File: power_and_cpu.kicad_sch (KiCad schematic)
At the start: 256 parts, among them J1 CPU1 USB, J10 AUX GPIO 1, J11 CAN2 PLUG, J12 Conn_01x06, J13 ADC AUX 2, J14 AUX GPIO 2, J15 AUX Encoder, J16 Conn_01x07, J17 CAN Output, J2 CAN Input, J21 Power Input, J3 Encoder 1, J4 Encoder 2, J5 Conn_01x06, J6 CPU2 USB, J7 Conn_01x02, J9 ADC AUX 1, Q7 Q_NMOS_GSD, SW1 SW_MEC_5G, SW2 SW_MEC_5G, SW3 CONFIG SWITCH, U10 TXS0101DCKR, U11 TLV1117LV33DCYR, U12 W25Q128JVSIQ, U13 W25Q128JVSIQ, U15 RP2040, U17 isolator, U18 MCP2515-xSO, U19 RP2040, U22 ADS7822U, U23 SN74LVC1G07QDCKTQ1, U24 MT2492, U25 NCP1117-5_SOT223, U26 ADC081S021CISD/NOPB, U27 USBLC6-2P6, U28 USBLC6-2P6, U29 USBLC6-4SC6, U3 USBLC6-4SC6, U30 USBLC6-4SC6, U31 USBLC6-4SC6, U32 TLV1117LV33DCYR, U33 TX4139, U34 LTV-208, U43 USBLC6-4SC6, U6 SN74LVC1G07QDCKTQ1, U9 ADC081S021CISD/NOPB, Y1 12MHz, Y2 12MHz, Y3 16MHz

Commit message: Rev 3.1 updated files. ordered Nov 2 2023
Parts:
- removed J7: Conn_01x02, parts:BOOMELE-2510-2A _1x02_P2.54mm_Vertical, symbol Connector_Generic:Conn_01x02
- removed U25: NCP1117-5_SOT223, Package_TO_SOT_SMD:SOT-223-3_TabPin2, symbol Regulator_Linear:NCP1117-3.3_SOT223
- added J8: Estop Conn, parts:BOOMELE-2510-3A_1x03_P2.54mm_Vertical, symbol Connector_Generic:Conn_01x03
- added JP1: SolderJumper_2_Open, Jumper:SolderJumper-2_P1.3mm_Open_RoundedPad1.0x1.5mm, symbol Jumper:SolderJumper_2_Open
- C87, C88, C89, C90, C91, C92: value C -> 22nF; LCSC (none) -> C77069; now fitted; now in the parts list
- C98: LCSC C106217 -> C779971
- D28, D29, D30, D32: LCSC C129213 -> C2841409
- D39: Digikey 67-1696-1-ND -> (none); LCSC C5137318 -> C84261; MPN SML-LX1206SOC-TR -> (none)
- J12, J3, J4, J5: LCSC C140771 -> C2982035
- J17, J2: now left out of the parts list
- J21: LCSC (none) -> C98733; now in the parts list
- R99: LCSC C22773 -> C2933129
- TP22: LCSC C238130 -> C5199800
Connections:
- net ADC_CS3 is gone; now on net ADC_CS2: U19.5 (GPIO3), U26.6 (~{CS})
- net ADC_CS2: no longer U19.3 (GPIO1), U9.6 (~{CS})
- net CAN0_N: no longer JP2.1 (A)
- net CANH0_P_JP: no longer JP2.2 (B)
- net ESTOP_SWITCH_IN: now also J8.3 (Pin_3)
- net ESTOP_SWITCH_OUT: now also J8.1 (Pin_1)
- net GND: now also J21.1 (Pin_1), JP2.1 (A), JP1.1 (A); no longer C87.1, C88.2, C89.2, C90.1, C91.1, C92.1, J21.2 (Pin_2)
- net VMOT: now also J21.2 (Pin_2); no longer J21.1 (Pin_1)
- net GPIO28_ADC2_2 renamed TH_MOTOR1
- net GPIO29_ADC3_2 renamed TH_MOTOR2
- net VDC_DATA renamed GPIO23
- new net ADC_CS1: U19.3 (GPIO1), U9.6 (~{CS})
- new net ENC1_JP: C87.1, C88.2, C89.2, JP1.2 (B)
- new net ENC2_JP: C90.1, C91.1, C92.1, JP2.2 (B)
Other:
- note added: "Jumpers enable additional filtering for hall sensors."
- note removed: "Backup footprint if new 5v switcher does not work properly."
- note removed: "These DNP caps are optional filter caps for hall sensors."
- moved on the sheet: R74

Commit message: Update to Rev 3.2. Probably okay to order this rev.
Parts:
- removed TP1, TP3: TestPoint, TestPoint:TestPoint_Pad_1.0x1.0mm, symbol Connector:TestPoint
- added C67: 100n, Capacitor_SMD:C_0603_1608Metric, symbol Device:C
- added D45: 10V Zener, Diode_SMD:D_SOD-123, symbol Device:D_Zener
- added D46: 7.5V Zener, Diode_SMD:D_SOD-123, symbol Device:D_Zener
- added Q10: AO3401A, Package_TO_SOT_SMD:SOT-23, symbol Transistor_FET:AO3401A
- added Q11: L2N7002SWT1G, Package_TO_SOT_SMD:SOT-323_SC-70, symbol Transistor_FET:AO3400A
- added Q8: Q_NMOS_GSD, Package_TO_SOT_SMD:SOT-23, symbol Device:Q_NMOS_GSD
- added Q9: AO3400A, Package_TO_SOT_SMD:SOT-23, symbol Transistor_FET:AO3400A
- added R100: 120R, Resistor_SMD:R_0603_1608Metric, symbol MotorController:TAYLOR_RESISTOR
- added R102: 20k, Resistor_SMD:R_0603_1608Metric, symbol MotorController:TAYLOR_RESISTOR
- added R103, R106: 100k, Resistor_SMD:R_0603_1608Metric, symbol MotorController:TAYLOR_RESISTOR
- added R104, R107, R137, R138: 10k, Resistor_SMD:R_0603_1608Metric, symbol MotorController:TAYLOR_RESISTOR
- added SW4: SW_DIP_x01, parts:SW-SMD_DSHP01TSGER, symbol Switch:SW_DIP_x01
- added U16: ~, Package_SO:SOP-4_4.4x2.6mm_P1.27mm, symbol Isolator:SFH617A-1X007T
- added U25: SN74LVC1G07QDCKTQ1, Package_TO_SOT_SMD:SOT-353_SC-70-5, symbol acorn-motherboard:SN74LVC1G07QDCKTQ1
- added U35: PCA9557PW, Package_SO:TSSOP-16_4.4x5mm_P0.65mm, symbol Interface_Expansion:PCA9557PW
- U26, U9: symbol 2022-06-16_01-48-54:ADC081S021CISD/NOPB -> 2022-06-16_01-48-54:ADC081S021CISD/NOPB
- renumbered C26 to C120
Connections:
- net +12V: now also D46.1 (K), Q10.2 (S), R106.1; no longer U24.4 (EN)
- net +3V3: now also C67.1, R137.2, U25.2 (A), U25.5 (VCC), U35.16 (VDD)
- net +5V_ISO: now also R100.1
- net GND: now also C67.2, D45.2 (A), Q11.2 (S), Q8.2 (S), Q9.2 (S), R103.2, R107.2, R138.2, U16.3, U25.3 (GND), U35.3 (A0), U35.4 (A1), U35.5 (A2), U35.8 (VSS); no longer D33.1 (GND), D34.1 (GND), D35.1 (GND)
- net GND_ISO: now also U16.2
- net ID1: now also U35.6 (IO0); no longer U19.29 (GPIO18)
- net ID2: now also U35.7 (IO1); no longer U19.30 (GPIO19)
- net ID3: now also U35.9 (IO2); no longer U19.35 (GPIO23)
- net VMOT: now also R102.1
- net /LED_EN: now also U25.1 (/OE)
- net ~{EN}: now reaches U33.6 (EN)
- net ~{EN}: now also SW4.2
- net 12V_POK: now reaches U33.7 (POK)
- net 12V_POK: now also U24.4 (EN), R106.2
- net DRIVER_ENABLE: now reaches U19.7 (GPIO5)
- net DRIVER_ENABLE: now also Q9.1 (G), R107.1
- new net: D45.1 (K), Q8.1 (G), R102.2, R103.1, U16.4
- new net: Q9.3 (D), R104.2
- new net: R100.2, U16.1
- new net: Q11.1 (G), R138.1, U25.4 (Y)
- new net: R137.1, U35.15 (~{RESET})
- new net: D46.2 (A), Q10.1 (G), R104.1
- new net: Q8.3 (D), SW4.1
- new net 12V_SWITCHED: Q10.3 (D)
- new net SCL1: U19.30 (GPIO19), U35.1 (SCL)
- new net SDA1: U19.29 (GPIO18), U35.2 (SDA)
- new net WS2812_SINK: D33.1 (GND), D34.1 (GND), D35.1 (GND), Q11.3 (D)
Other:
- moved on the sheet: C19, C42, C43, C44, C45, C46, C47, C48, C49, C50, C51, C52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

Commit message: Latest updates to module based design.
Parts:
- removed D46: 7.5V Zener, Diode_SMD:D_SOD-123, symbol Device:D_Zener
- removed H1, H2, H6, H7, H8: MountingHole, RP2040_minimal:MountingHole_3.9mm_Plastite_#6, symbol Mechanical:MountingHole
- removed J16: Conn_01x07, Connector_PinHeader_2.54mm:PinHeader_2x04_P2.54mm_Vertical, symbol Connector_Generic:Conn_01x07
- removed J21: Power Input, Connector_AMASS:AMASS_XT60-F_1x02_P7.20mm_Vertical, symbol Connector_Generic:Conn_01x02
- removed Q10: AO3401A, Package_TO_SOT_SMD:SOT-23, symbol Transistor_FET:AO3401A
- removed Q9: AO3400A, Package_TO_SOT_SMD:SOT-23, symbol Transistor_FET:AO3400A
- removed R104, R107: 10k, Resistor_SMD:R_0603_1608Metric, symbol MotorController:TAYLOR_RESISTOR
- removed TH1, TH2: Thermistor 10k, Resistor_SMD:R_0603_1608Metric, symbol Device:Thermistor_NTC
- removed TP49, TP51: TestPoint, TestPoint:TestPoint_Pad_D2.0mm, symbol Connector:TestPoint
- added JP10: SolderJumper_3_Open, Jumper:SolderJumper-3_P1.3mm_Open_RoundedPad1.0x1.5mm, symbol Jumper:SolderJumper_3_Open
- added JP4, JP5, JP8, JP9: SolderJumper_2_Open, Jumper:SolderJumper-2_P1.3mm_Open_RoundedPad1.0x1.5mm, symbol Jumper:SolderJumper_2_Open
- added U1, U2: ~, driver_module:driver_module, symbol driver_module:Driver
- added U4: TXS0101DCKR, Package_TO_SOT_SMD:SOT-363_SC-70-6, symbol MotorBuck:level_shifter
- C120: footprint Capacitor_THT:CP_Radial_D8.0mm_P3.50mm -> Capacitor_SMD:CP_Elec_8x10.5; LCSC C2887234 -> C5246568
- J10, J13, J14, J9: footprint parts:BOOMELE-2510-3A_1x03_P2.54mm_Vertical -> parts:CONN-TH_3P-P2.54_HCTL_HC-2510-3AW; LCSC C509148 -> C2982042
- J15: footprint parts:BOOMELE-2510-5A _1x05_P2.54mm_Vertical -> parts:CONN-TH_5P-P2.54_HCTL_HC-2510-5AW; LCSC C27544 -> C2982044
- SW1, SW2: footprint parts:SW_TS_1101_C_W -> parts:KEY-SMD_1TS002G; LCSC C318938 -> C319375
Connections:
- net +12V: now also U1.5 (+12V), U2.5 (+12V)
- net +3.3VA: now also U1.7 (+3V3), U2.7 (+3V3)
- net +3V3: now also JP10.1 (A), U4.1 (VCCA), U4.5 (OE); no longer J15.1 (Pin_1), TP34.1
- net +5V: now also JP10.3 (B)
- net AUX3_SCK: now also U4.3 (A); no longer J15.4 (Pin_4), TP37.1
- net GND: now also JP4.1 (A), JP5.1 (A), JP8.1 (A), JP9.1 (A), U1.1 (GND), U1.12 (GND), U1.2 (Thermistor), U1.21 (GND), U1.22 (GND), U1.25 (GND), U1.26 (GND), U2.1 (GND), U2.12 (GND), U2.2 (Thermistor), U2.21 (GND), U2.22 (GND), U2.25 (GND), U2.26 (GND), U4.2 (GND)
- net M1A_PWM_H: now also U1.16 (PWM_A_H)
- net M1A_PWM_L\: now also U1.18 (PWM_A_L\)
- net M1A_SENSE: now also U1.19 (SENSE_A)
- net M1B_PWM_H: now also U1.20 (PWM_B_H)
- net M1B_PWM_L\: now also U1.17 (PWM_B_L\)
- net M1C_PWM_H: now also U1.8 (PWM_C_H)
- net M1C_PWM_L\: now also U1.6 (PWM_C_L\)
- net M1C_SENSE: now also U1.9 (SENSE_C)
- net M2A_PWM_H: now also U2.16 (PWM_A_H)
- net M2A_PWM_L\: now also U2.18 (PWM_A_L\)
- net M2A_SENSE: now also U2.19 (SENSE_A)
- net M2B_PWM_H: now also U2.20 (PWM_B_H)
- net M2B_PWM_L\: now also U2.17 (PWM_B_L\)
- net M2C_PWM_H: now also U2.8 (PWM_C_H)
- net M2C_PWM_L\: now also U2.6 (PWM_C_L\)
- net M2C_SENSE: now also U2.9 (SENSE_C)
- net VMOT: now also U1.11 (VMOT), U1.13 (VMOT), U1.23 (VMOT), U1.24 (VMOT), U2.11 (VMOT), U2.13 (VMOT), U2.23 (VMOT), U2.24 (VMOT)
- net Bridge_TH_1: now reaches R45.1, U9.3 (VIN)
- net Bridge_TH_1: now also U1.2 (Thermistor)
- net Bridge_TH_2: now reaches R21.1, U26.3 (VIN)
- net Bridge_TH_2: now also U2.2 (Thermistor)
- net DRIVER_ENABLE: no longer names the net of U19.7 (GPIO5)
- removed net ENC1_JP: C87.1, C88.2, C89.2, JP1.2 (B)
- removed net ENC2_JP: C90.1, C91.1, C92.1, JP2.2 (B)
- new net: C90.1, JP4.2 (B)
- new net: C89.2, JP2.2 (B)
- new net: C91.1, JP5.2 (B)
- new net: C87.1, JP9.2 (B)
- new net: C88.2, JP8.2 (B)
- new net: C92.1, JP1.2 (B)
- new net AUX3_SCK_SHIFTED: J15.4 (Pin_4), TP37.1, U4.4 (B)
- new net AUXV: J15.1 (Pin_1), JP10.2 (C), TP34.1, U4.6 (VCCB)
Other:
- moved on the sheet: C23, C60, C61, C62, C63, C90, C91, C92

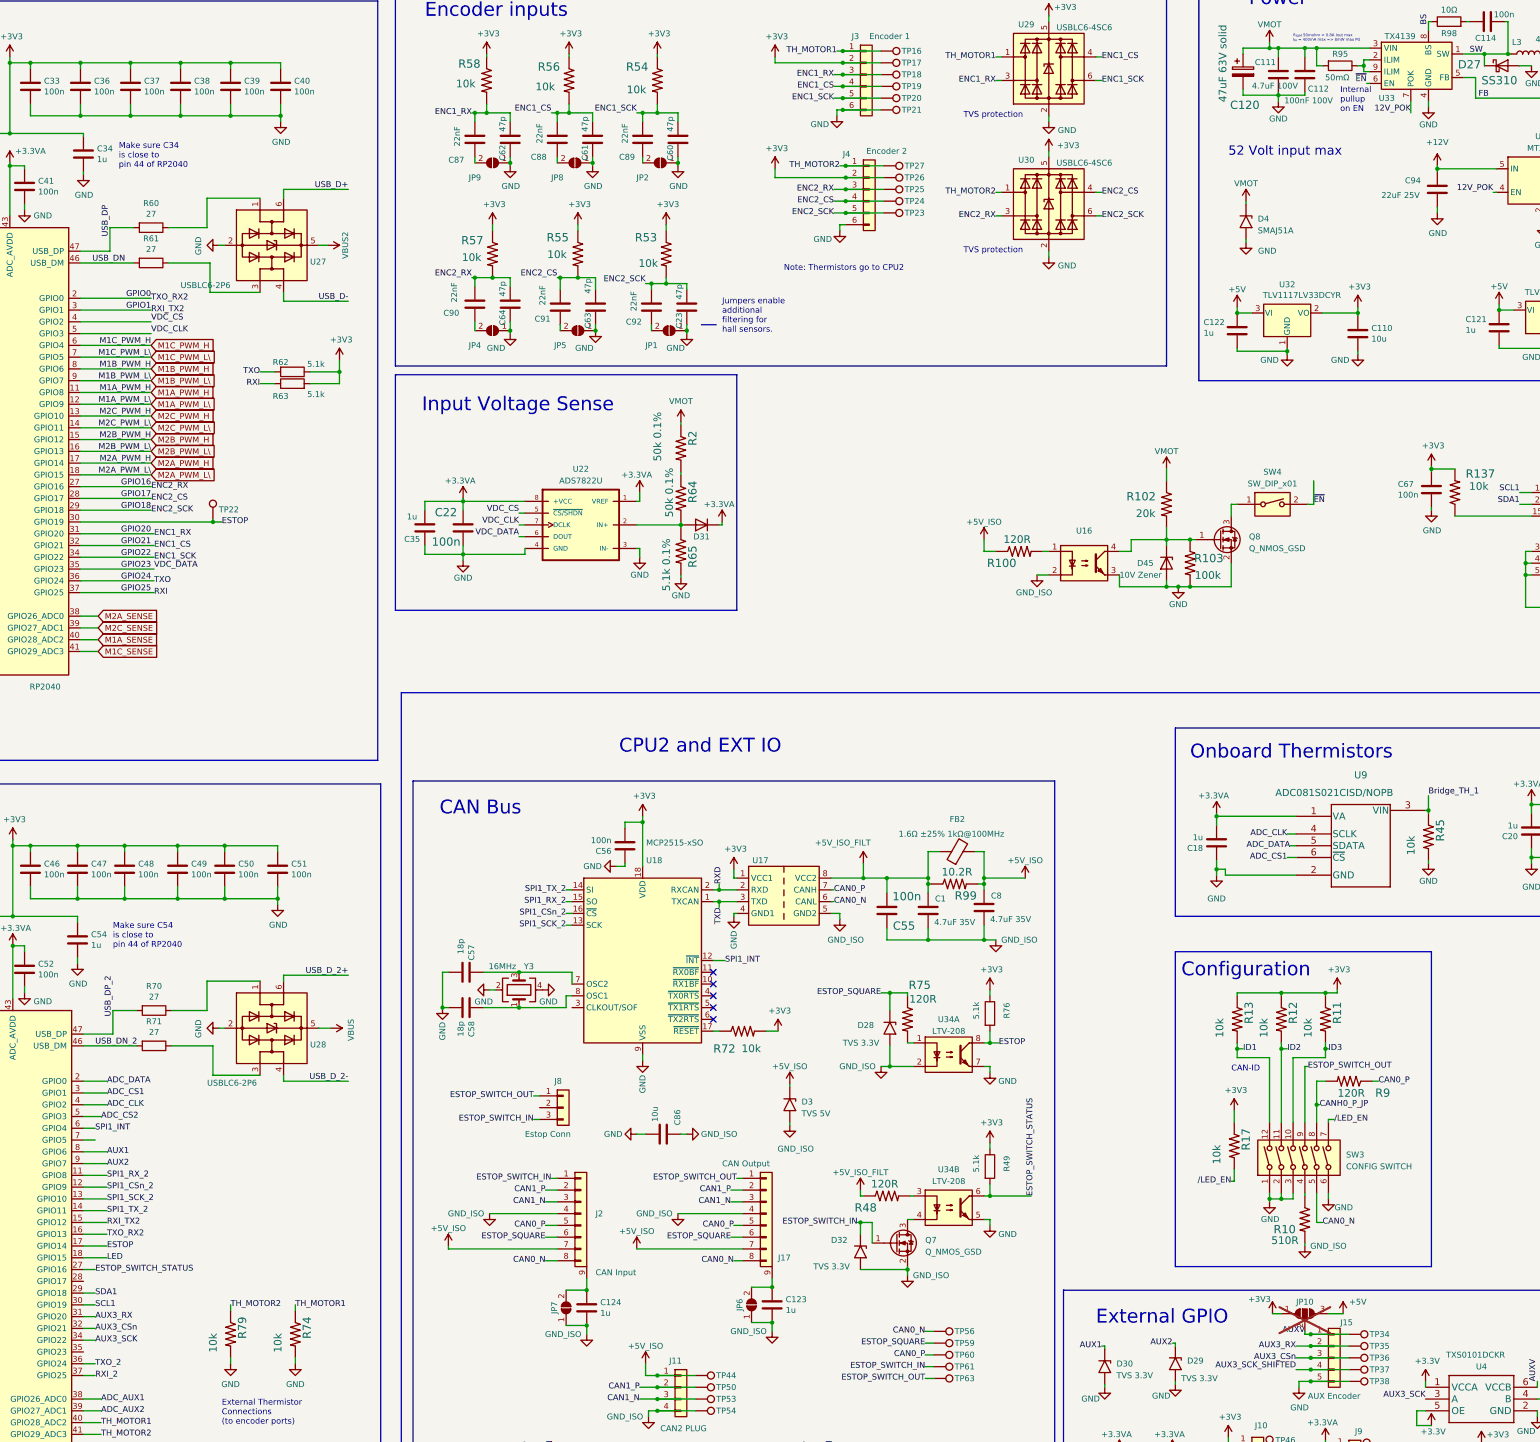
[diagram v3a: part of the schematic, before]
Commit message: Driver module and main board initial 100% layout
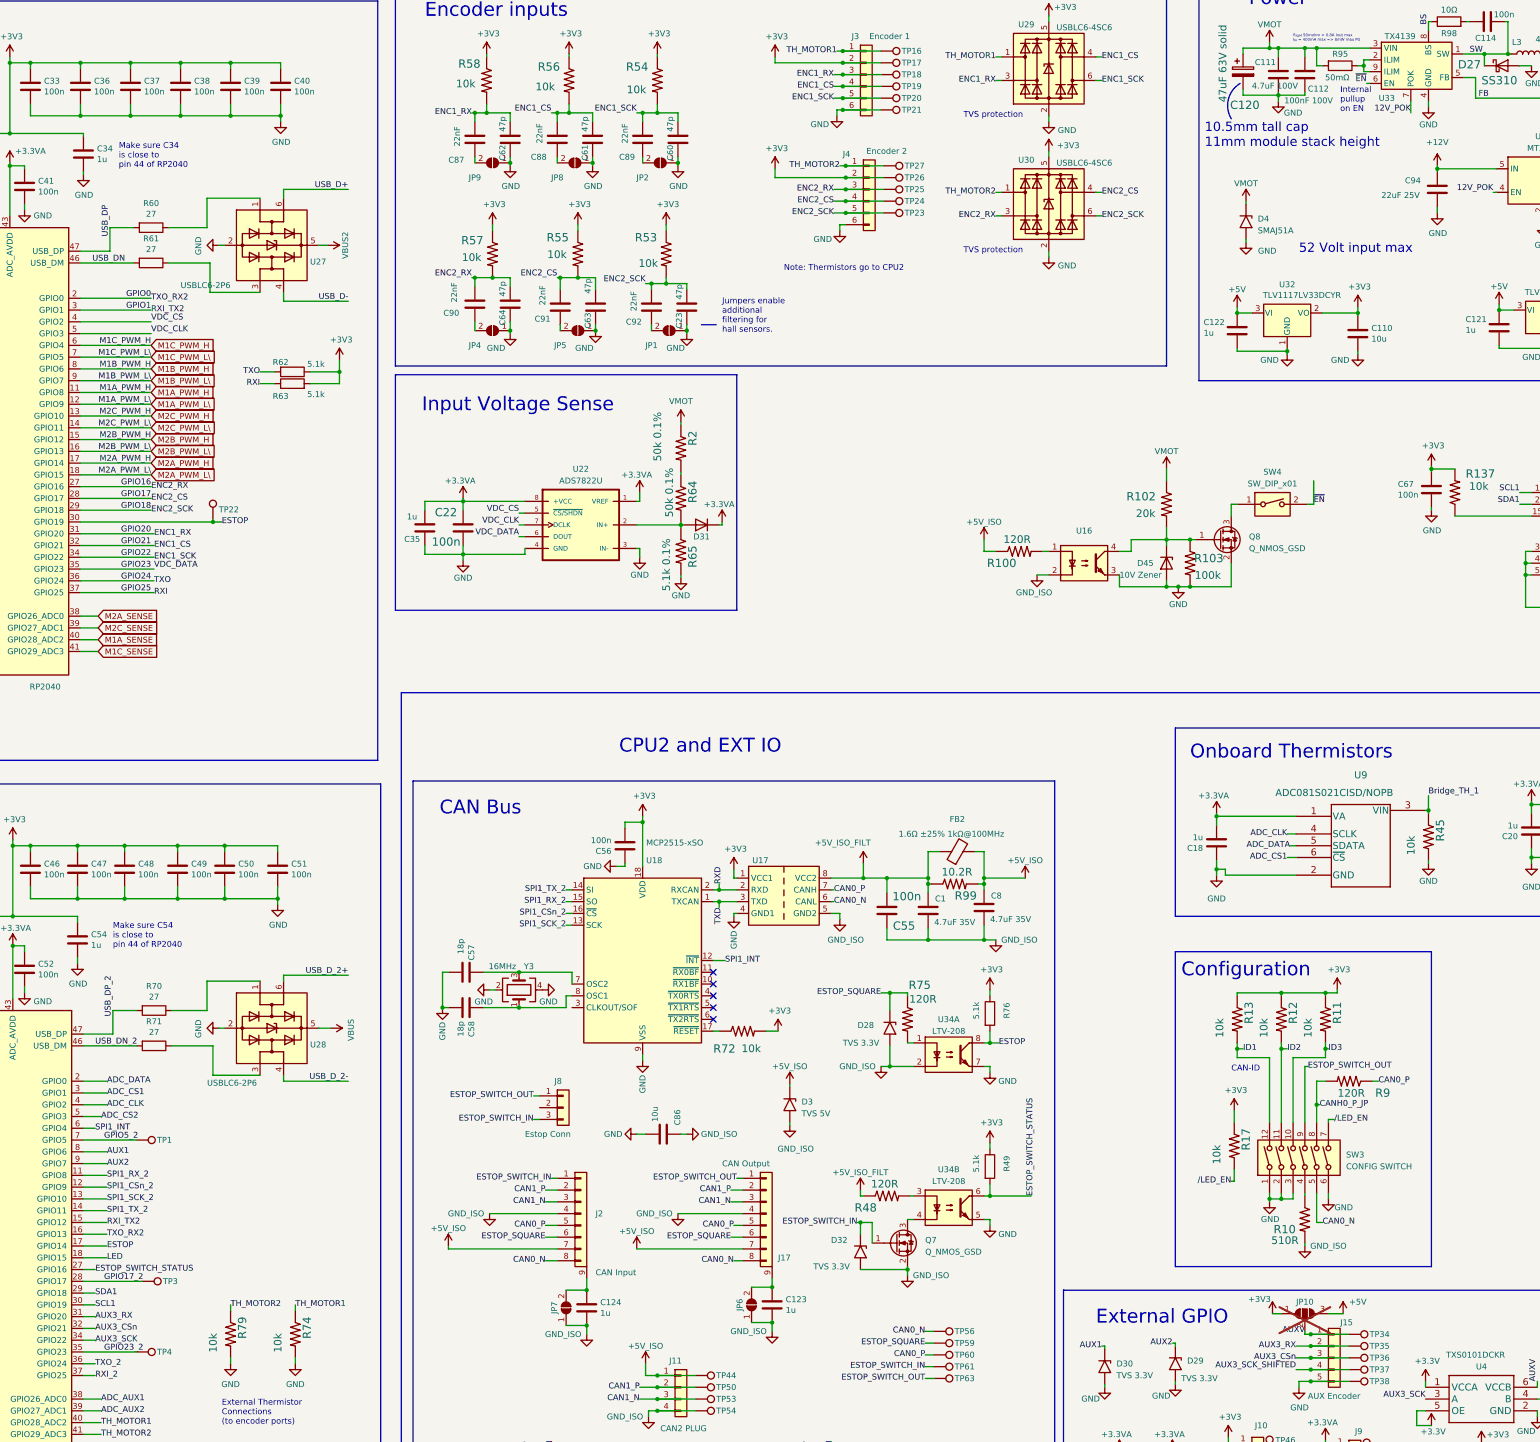
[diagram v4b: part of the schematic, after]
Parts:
- added TP1, TP3, TP4: TestPoint, TestPoint:TestPoint_Pad_D1.0mm, symbol Connector:TestPoint
- TP10, TP11, TP13, TP14, TP15, TP16, TP17, TP18, TP19, TP20, TP21, TP23, TP24, TP25, TP26, TP27, TP28, TP29, TP30, TP31, TP32, TP33, TP34, TP35, TP36, TP37, TP38, TP39, TP40, TP41, TP42, TP43, TP44, TP45, TP46, TP47, TP48, TP50, TP52, TP53, TP54, TP56, TP59, TP60, TP61, TP63: footprint TestPoint:TestPoint_Pad_D2.0mm -> TestPoint:TestPoint_Pad_D1.0mm
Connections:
- net GPIO17_2: now reaches U19.28 (GPIO17)
- net GPIO17_2: now also TP3.1
- net GPIO23_2: now reaches U19.35 (GPIO23)
- net GPIO23_2: now also TP4.1
- net GPIO5_2: now reaches U19.7 (GPIO5)
- net GPIO5_2: now also TP1.1
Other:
- note added: "10.5mm tall cap 11mm module stack height"

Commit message: Significant clean up of base board and driver module. potentially orderable.
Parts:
- removed R21, R45: 10k, Resistor_SMD:R_0603_1608Metric, symbol MotorController:TAYLOR_RESISTOR
- added J16, J19, J20, J7: Conn_02x05_Odd_Even, Connector_PinSocket_2.54mm:PinSocket_2x05_P2.54mm_Vertical, symbol Connector_Generic:Conn_02x05_Odd_Even
- added J18, J21: Conn_01x06, Connector_PinSocket_2.54mm:PinSocket_1x06_P2.54mm_Vertical, symbol Connector_Generic:Conn_01x06
- added R1, R3, R4, R5, R6, R7: ~, Resistor_SMD:R_0603_1608Metric, symbol MotorController:TAYLOR_RESISTOR
- J11: LCSC C402777 -> C2982033
- J17, J2: now in the parts list
- R95: LCSC C126169 -> C158894
- U1, U2: now not fitted; now left out of the parts list
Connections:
- net +3V3: now also R1.1, R3.1, R4.1, R5.1, R6.1, R7.1
- net ENC1_CS: now also R3.2
- net ENC1_RX: now also R4.2
- net ENC1_SCK: now also R1.2
- net ENC2_CS: now also R6.2
- net ENC2_RX: now also R5.2
- net ENC2_SCK: now also R7.2
